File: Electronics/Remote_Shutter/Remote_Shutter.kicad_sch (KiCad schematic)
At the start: 6 parts

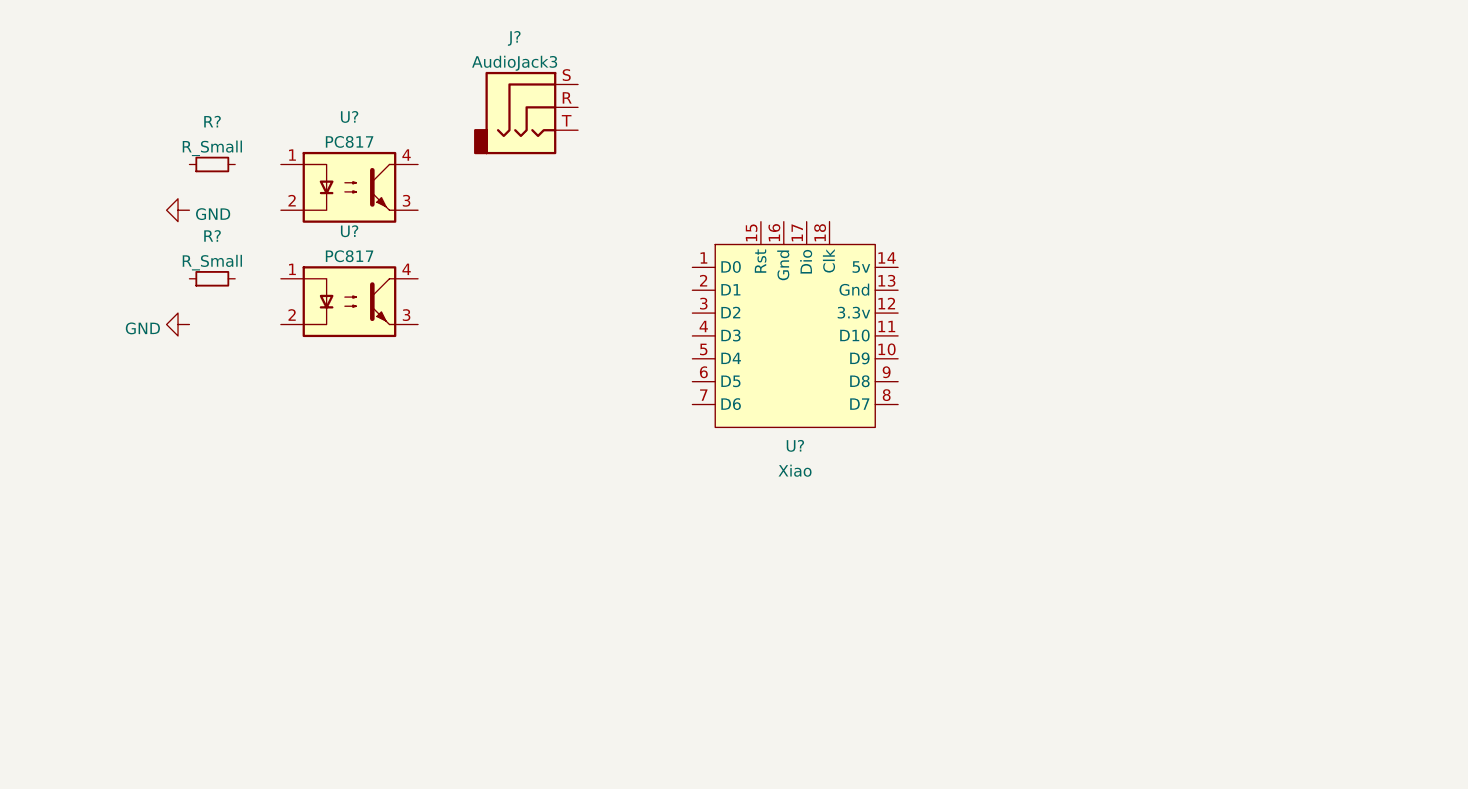
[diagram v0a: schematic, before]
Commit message: updating the schems and adding comments
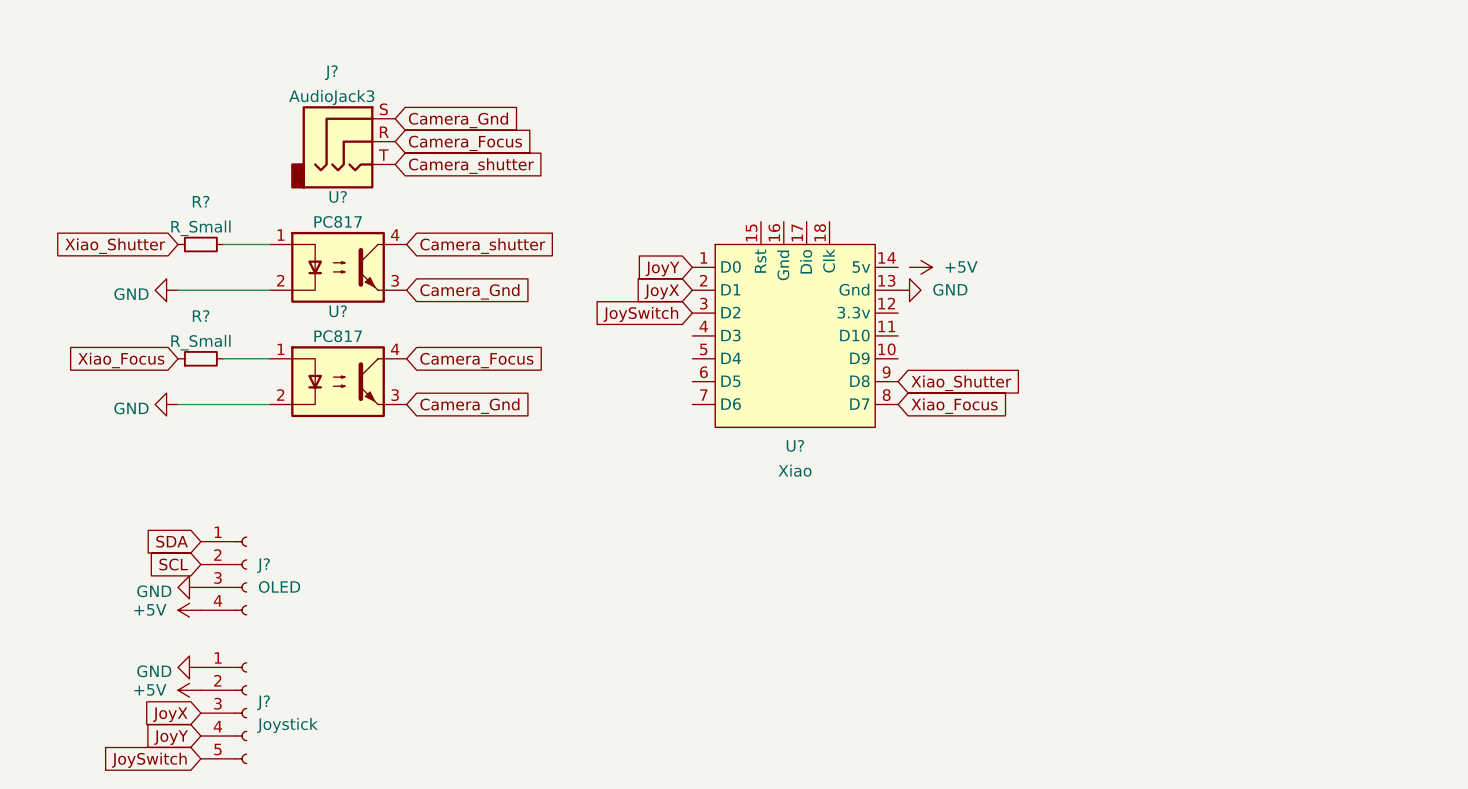
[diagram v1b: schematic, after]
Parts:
- added J?: OLED, symbol Connector:Conn_01x04_Female
- added J?: Joystick, symbol Connector:Conn_01x05_Female
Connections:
- net GND: now also U?.13 (Gnd), U?.2, U?.2, J?.1 (Pin_1), J?.3 (Pin_3)
- net at U?.1: now also R?.2
- net Camera_Gnd: now reaches U?.3
- net Camera_Gnd: now also J?.S, U?.3
- net Camera_Focus: now reaches U?.4
- net Camera_Focus: now also J?.R
- net Xiao_Focus: now reaches R?.1
- net Xiao_Focus: now also U?.8 (D7)
- net Xiao_Shutter: now reaches R?.1
- net Xiao_Shutter: now also U?.9 (D8)
- net at R?.2: now also U?.1
- net Camera_shutter: now reaches U?.4
- net Camera_shutter: now also J?.T
- net JoyY: now reaches U?.1 (D0)
- net JoyY: now also J?.4 (Pin_4)
- net JoyX: now reaches U?.2 (D1)
- net JoyX: now also J?.3 (Pin_3)
- net JoySwitch: now reaches U?.3 (D2)
- net JoySwitch: now also J?.5 (Pin_5)
- new net +5V: J?.2 (Pin_2), J?.4 (Pin_4)
- new net SCL: J?.2 (Pin_2)
- new net SDA: J?.1 (Pin_1)
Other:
- moved on the sheet: J?, R?, U?

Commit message: Mostly finished the circuit diagram
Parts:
- added J?: Micro Lipo pins, symbol Connector:Conn_01x02_Female
- R? (x2): value R_Small -> 220ohm
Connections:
- net +5V: now also U?.14 (5v), J?.1 (Pin_1); no longer J?.2 (Pin_2)
- net GND: now also J?.2 (Pin_2)
- net SCL: now also U?.6 (D5)
- net SDA: now also U?.5 (D4)
- net +3V3: now reaches U?.12 (3.3v)
- net +3V3: now also J?.2 (Pin_2)
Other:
- note added: "Galvanic Isolation"
- note added: "Local to Camera"
- note added: "Local to Xiao"
- moved on the sheet: J?, R?, U?

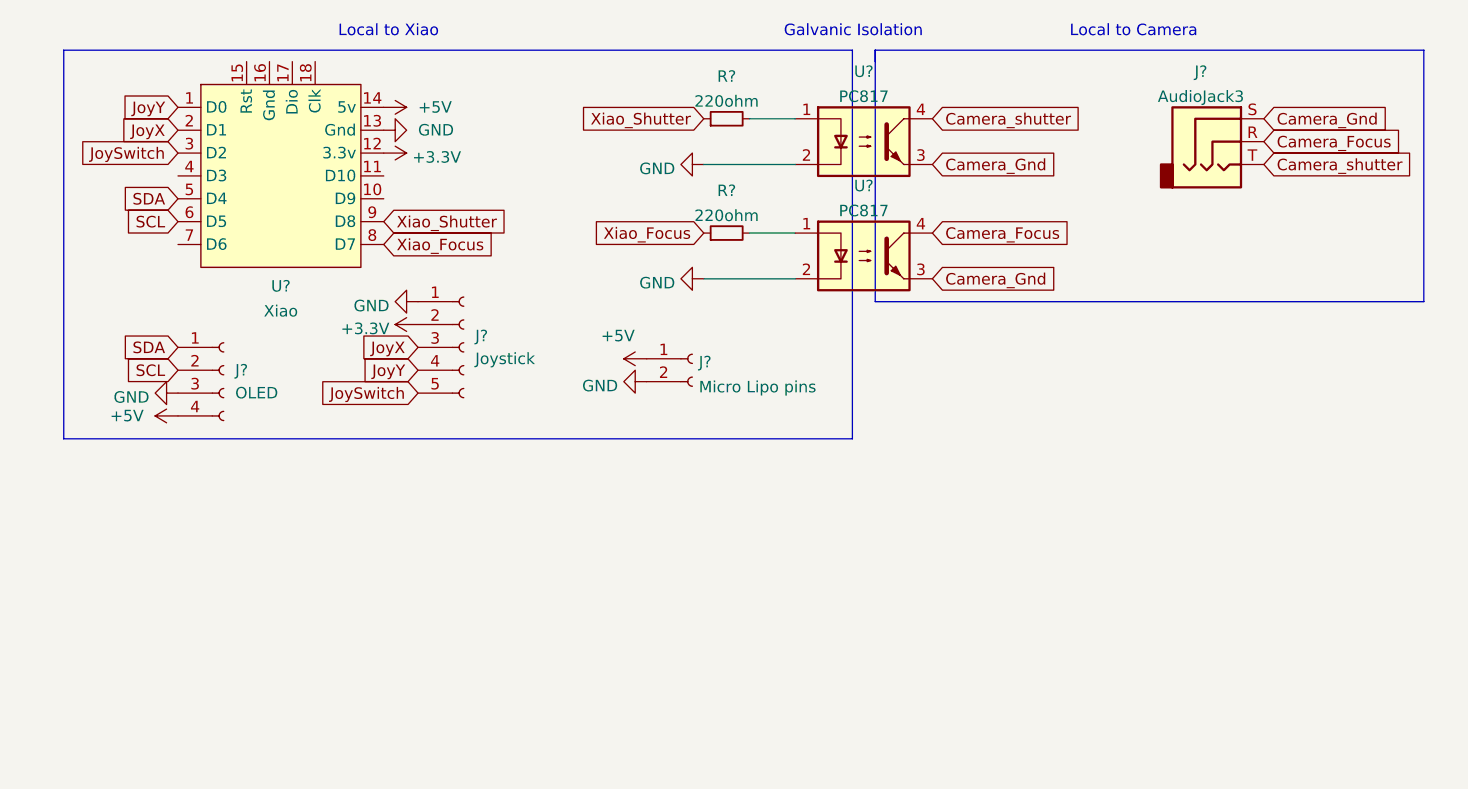
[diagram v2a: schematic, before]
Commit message: added indicator leds
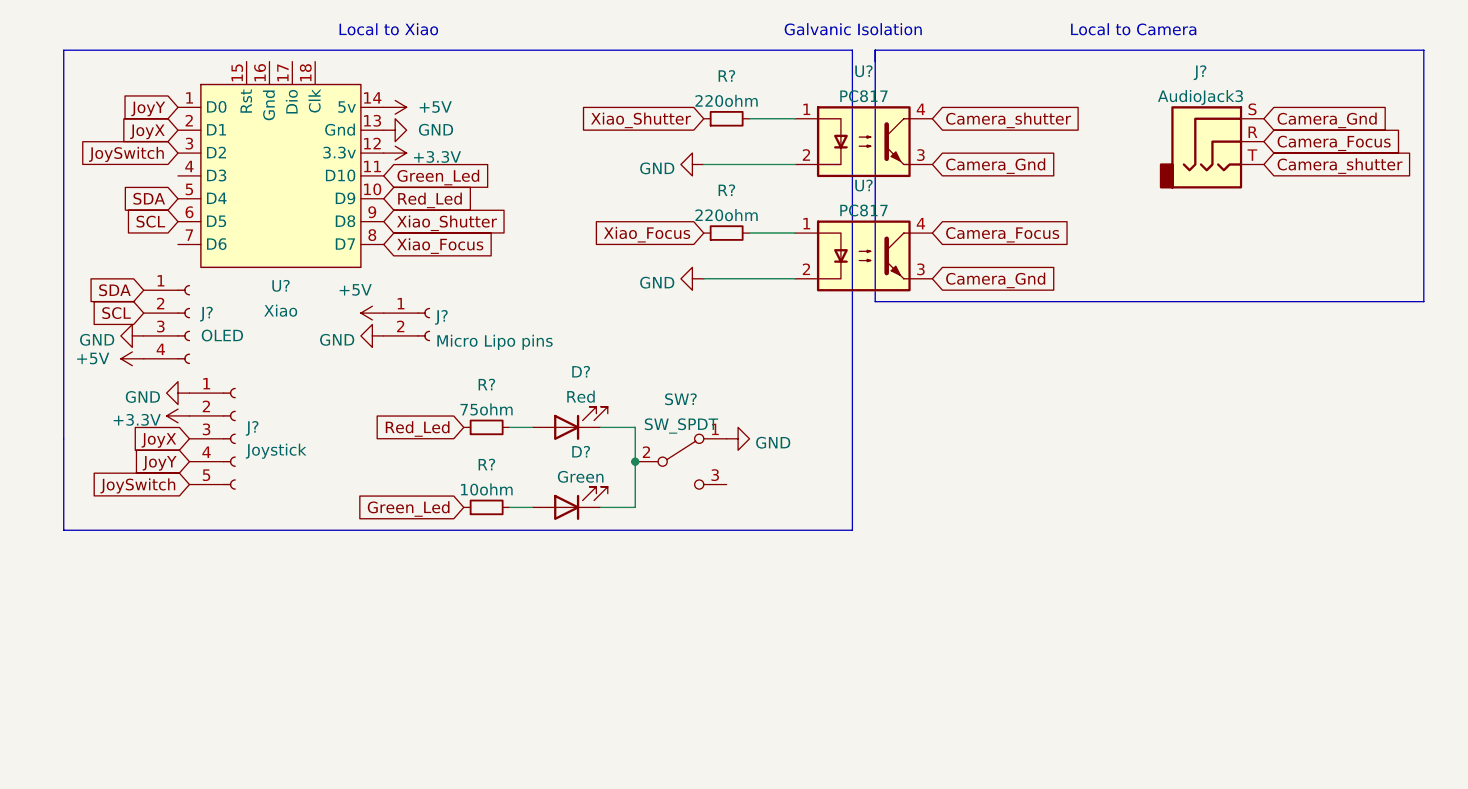
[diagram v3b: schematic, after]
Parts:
- added D?: Green, symbol Device:LED
- added D?: Red, symbol Device:LED
- added R?: 75ohm, symbol Device:R_Small
- added R?: 10ohm, symbol Device:R_Small
- added SW?: SW_SPDT, symbol Switch:SW_SPDT
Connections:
- net GND: now also SW?.1 (A)
- net Red_Led: now reaches U?.10 (D9)
- net Red_Led: now also R?.1
- net Green_Led: now reaches U?.11 (D10)
- net Green_Led: now also R?.1
- new net: D?.1 (K), D?.1 (K), SW?.2 (B)
- new net: D?.2 (A), R?.2 (x2)
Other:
- moved on the sheet: J?

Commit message: PCB design
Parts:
- added SW2: SW_SPDT, Button_Switch_SMD:SW_SPDT_PCM12, symbol Switch:SW_SPDT
- D1, D2: renamed from D?; footprint (none) -> LED_THT:LED_D3.0mm
- J1: renamed from J?; footprint (none) -> Connector_PinSocket_2.54mm:PinSocket_1x04_P2.54mm_Vertical
- J2: renamed from J?; footprint (none) -> Connector_PinSocket_2.54mm:PinSocket_1x05_P2.54mm_Vertical
- J3: renamed from J?; footprint (none) -> Connector_PinSocket_2.54mm:PinSocket_1x02_P2.54mm_Vertical
- J4: renamed from J?; footprint (none) -> cubepattern:CUI_SJ1-3514
- R1, R2, R3, R4: renamed from R?; footprint (none) -> Resistor_THT:R_Axial_DIN0207_L6.3mm_D2.5mm_P10.16mm_Horizontal
- SW1: renamed from SW?; footprint (none) -> Button_Switch_SMD:SW_SPDT_PCM12
- U1: renamed from U?; footprint (none) -> cubepattern:Seeeduino XIAO-MOUDLE14P-2.54-21X17.8MM tht maybe no pads
- gave numbers to parts that had none: 2
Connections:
- net +5V: now also J1.3 (Pin_3), SW2.2 (B); no longer J1.4 (Pin_4), J3.1 (Pin_1)
- net GND: now also J1.4 (Pin_4); no longer J1.3 (Pin_3)
- new net: J3.1 (Pin_1), SW2.3 (C)
- no-connect marks 0 -> 4
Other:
- moved on the sheet: J3
